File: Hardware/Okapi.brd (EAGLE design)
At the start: 64.8 x 100 mm, 215 parts, among them IC1 ATMEGA1284M, J1 CONN_82.54_SCREW, J3 CONN_42.54_SCREW, J4 CONN_82.54_SCREW, Q1 DMG3404, Q2 DMG3404, Q3 FDN360P, Q4 2N7002, Q5 FDN360P, Q6 DMG3404, Q7 2N7002, Q8 2N7002, U1 TLV61220DBV, U10 TPS22917DBV, U11 SN74AUP1G04YFP, U12 SN74AUP1G04YFP, U13 SN74AUP1G04YFP, U14 SN74AUP2G08DQE, U15 SN74AUP2G08DQE, U16 SN74AUP2G08DQE, U17 MIC2544MSOP, U18 MIC2544MSOP, U19 MIC2544MSOP, U2 TPS62822DLC, U20 MIC2544MSOP, U21 TPS22917DBV, U22 TPS22917DBV, U23 FT231X-Q, U24 SN74LVC1G3157DRL, U25 SN74AUP3G34DCU, U26 TXS0102DQM, U27 TXS0104RGY, U28 TCA9406DCU, U29 TXS0104RGY, U3 TPS61032RSA, U30 MCP4726A2SOT-23, U31 BME280, U32 ADS1115, U33 ADS1115, U34 INA211DCK, U35 INA213DCK, U36 TCA9406DCU, U37 TLV3691DCK, U38 TS5A21366RSE, U39 MIC94094C6, U40 SN74AHC1G86DCK, U41 MCP23018QFN, U42 TXS0104RGY, U5 BQ2980RUG, U6 TPS2105, U7 LTC4412S6, U8 TPL5111DDC, U9 TPS79733

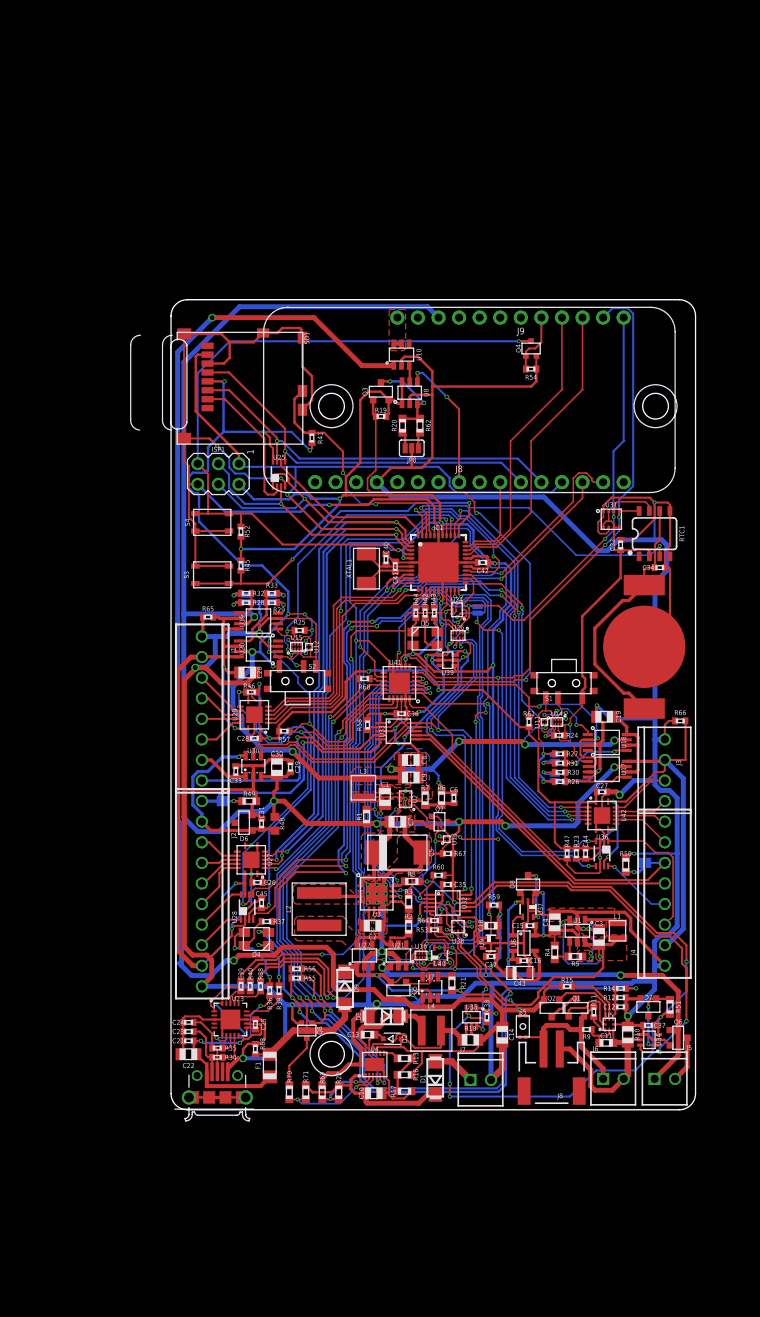
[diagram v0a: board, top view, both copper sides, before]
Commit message: Updated layout
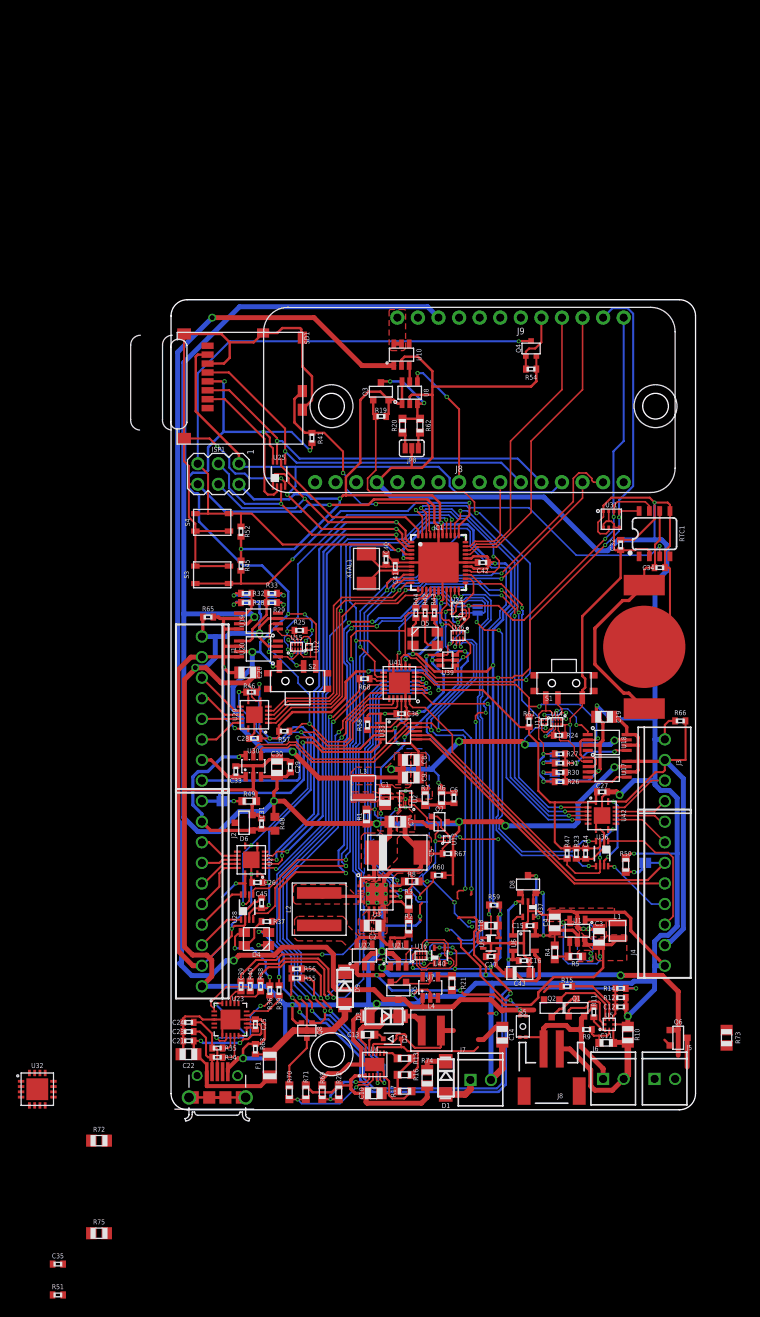
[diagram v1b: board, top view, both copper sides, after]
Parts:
- removed C37, C38: 0.1uF, bschulz_passives:C0402
- removed D7: (no value), bschulz:SOT23-3
- removed R18: 50m, bschulz_passives:R0805
- removed R53, R64: 1M, bschulz_passives:R0402
- removed U34: INA211DCK, bschulz:DCK_R-PDSO-G6
- removed U35: INA213DCK, bschulz:DCK_R-PDSO-G6
- removed U38: TS5A21366RSE, bschulz:RSE0008A
- added R72, R73, R74, R75: (no value), bschulz_passives:R0805
- R51: value 20k -> (none); device bschulz_passives:R0603 -> bschulz_passives:R0402
- U32: value ADS1115 -> PAC1934QFN; device bschulz:VSSOP_10 -> bschulz:QFN16
- moved R51 83.5 mm to (-14.0, -22.9), turned to 0 degrees
- moved C35 67.2 mm to (-14.0, -19.1), turned to 0 degrees
- moved U32 55.6 mm to (-16.5, 2.54), turned to 0 degrees
- moved D1 1.27 mm to (33.9, 3.94), turned to 270 degrees
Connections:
- removed net I_LI: U32.7, U34.6
- removed net I_SOLAR: U32.5, U35.6
- removed net SOLAR_SENSE+: L4.P$2, R18.1, U35.4, U4.10
- new net CSA_!ALERT: U32.1, U41.4
- new net V_BETA_SENSE: D9.C, Q5.2, R75.1, U32.10
- new net V_SOLAR_SENSE: D1.C, R74.1, U32.8
- net 3V3_CORE: now also C35.1, U32.15, U32.16, U32.2
- net 5V_AUX: no longer C35.1, C37.1, C38.1, R51.2, U32.8, U34.3, U35.3, U38.2
- net ADC_OB_ALERT: no longer U32.2, U41.4
- net ADC_SENSE_SW: no longer U38.3, U38.7
- net GND: now also R51.1, U32.EP; no longer C37.2, C38.2, D7.2, R53.1, R64.1, U32.1, U34.2, U34.4, U35.1, U35.2, U38.6
- net LI-: no longer U34.5
- net N$21: now also R51.2, U32.6; no longer D7.1, R51.1, U34.1
- net SCL: now also U32.4
- net SCL_5V: no longer U32.10
- net SDA_5V: no longer U32.9
- net SDA_OB: now also U32.5
- net V_BETA: now also R75.2, U32.9; no longer D9.C, Q5.2
- net V_LI: now also L4.P$2, R72.2, U32.11, U4.10; no longer Q2.2, R18.2, U35.5, U38.8
- net V_LI_SENSE: now also Q2.2, R72.1, U32.12; no longer R64.2, U32.4, U38.1
- net V_PRIME: now also R73.2, U32.14; no longer J5.P2, U38.4
- net V_PRIME_SENSE: now also J5.P2, R73.1, U32.13; no longer R53.2, U32.6, U38.5
- net V_SOLAR_IN: now also R74.2, U32.7; no longer D1.C
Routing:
- net 5V_AUX: track 343.4 -> 246.4 mm, vias 18 -> 13
- net I_LI: track 48.5 -> 0.00 mm, vias 2 -> 0
- net GND: track 910.3 -> 888.0 mm
- net I_SOLAR: track 19.8 -> 0.00 mm, vias 2 -> 0
- net SOLAR_SENSE+: track 18.3 -> 0.00 mm
- net V_PRIME_SENSE: track 12.5 -> 0.00 mm, vias 2 -> 0
- net N$21: track 9.40 -> 0.00 mm, vias 2 -> 0
- net V_LI_SENSE: track 8.45 -> 0.00 mm, vias 2 -> 0
- net V_BETA: track 64.1 -> 56.6 mm
- net V_LI: track 206.9 -> 213.0 mm
- net V_PRIME: track 76.1 -> 71.6 mm
- net V_BETA_SENSE: track 0.00 -> 4.16 mm
- net V_SOLAR_SENSE: track 0.00 -> 3.30 mm
- net V_PRIME-: track 5.69 -> 3.60 mm
- net ADC_OB_ALERT: track 42.5 -> 41.0 mm
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
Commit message: Continued layout updates
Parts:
- moved R72 55.0 mm to (43.4, 13.1), turned to 180 degrees
- moved R75 44.9 mm to (24.1, 15.2)
- moved R73 9.41 mm to (59.2, 9.27), turned to 90 degrees
- moved Q5 8.75 mm to (20.3, 18.8), turned to 0 degrees
- moved C14 4.33 mm to (36.6, 9.65)
- moved R38 1.27 mm to (9.78, 15.2)
- moved R40 1.14 mm to (10.9, 15.2)
- moved D9 0.92 mm to (21.0, 14.2)
- moved C13 0.25 mm to (24.3, 9.02)
- moved D3 0.25 mm to (26.3, 11.3)
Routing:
- net N$45: track 3.80 -> 18.2 mm
- net V_LI: track 213.0 -> 202.6 mm, vias 4 -> 2
- net GND: track 888.0 -> 897.1 mm
- net TX: track 103.6 -> 95.3 mm
- net 3V3_CORE: track 271.4 -> 279.1 mm
- net V_PRIME: track 71.6 -> 65.9 mm
- net RX: track 106.4 -> 101.2 mm
- net V_BETA: track 56.6 -> 61.4 mm, vias 4 -> 6
- net V_PRIME_SENSE: track 0.00 -> 4.72 mm
- net VUSB_POWER: track 63.9 -> 59.6 mm
- net V_BETA_SENSE: track 4.16 -> 1.47 mm, vias 0 -> 1
- net MPPT_FAULT: track 65.8 -> 63.4 mm
- net MPPT_CHRG: track 66.6 -> 64.5 mm
- net V_PRIME-: track 3.60 -> 5.69 mm
- net N$47: track 7.43 -> 8.65 mm
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
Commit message: CSA layout
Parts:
- removed R60: 100k, bschulz_passives:R0402
- moved C35 68.3 mm to (34.8, 28.8), turned to 180 degrees
- moved R51 66.2 mm to (31.1, 25.7), turned to 90 degrees
- moved U32 56.2 mm to (34.8, 25.4), turned to 270 degrees
- moved C18 0.36 mm to (39.8, 23.0)
- moved U9 0.25 mm to (39.8, 20.6)
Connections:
- removed net ADC_OB_ALERT: R60.1
- net 5V_AUX: no longer R60.2
- net V_BETA: now also U32.7; no longer U32.9
- net V_BETA_SENSE: now also U32.8; no longer U32.10
- net V_LI: now also U32.13; no longer U32.11
- net V_LI_SENSE: now also U32.14; no longer U32.12
- net V_PRIME: now also U32.12; no longer U32.14
- net V_PRIME_SENSE: now also U32.11; no longer U32.13
- net V_SOLAR_IN: now also U32.9; no longer U32.7
- net V_SOLAR_SENSE: now also U32.10; no longer U32.8
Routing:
- net ADC_SENSE_SW: track 66.4 -> 0.00 mm, vias 5 -> 0
- net SDA_OB: track 78.6 -> 122.1 mm, vias 4 -> 6
- net ADC_OB_ALERT: track 41.0 -> 0.00 mm, vias 2 -> 0
- net V_PRIME_SENSE: track 4.72 -> 37.4 mm, vias 0 -> 2
- net CSA_!ALERT: track 0.00 -> 32.3 mm, vias 0 -> 2
- net V_BETA_SENSE: track 1.47 -> 30.7 mm, vias 1 -> 2
- net V_BETA: track 61.4 -> 87.5 mm, vias 6 -> 7
- net V_SOLAR_IN: track 22.4 -> 48.0 mm, vias 0 -> 2
- net SDA_5V: track 65.9 -> 40.6 mm, vias 3 -> 2
- net V_SOLAR_SENSE: track 3.30 -> 28.4 mm, vias 0 -> 2
- net SCL_5V: track 67.9 -> 44.0 mm, vias 3 -> 2
- net V_PRIME: track 65.9 -> 87.7 mm, vias 5 -> 6
- net V_LI_SENSE: track 0.00 -> 18.8 mm
- net V_LI: track 202.6 -> 220.1 mm
- net SCL: track 173.3 -> 185.8 mm, vias 6 -> 7
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
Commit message: Design updates toward v1.0
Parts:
- removed USB1: MICRO_USB_LONGPADS, bschulz:10118194-0001LF_10118194-0001LF_LONGER_PADS
- added C37, C38, C46, C47, C48, C50, C57: 0.1uF, bschulz_passives:C0402
- added D10, D13, D16: LEDGREEN0603, bschulz:LED_0603
- added D11, D14, D17: LEDYELLOW0603, bschulz:LED_0603
- added D12, D18: LEDRED0603, bschulz:LED_0603
- added D7: CLVBA-FKA, bschulz:CLVBA-FKA
- added F2: (no value), bschulz:1206
- added J10: (no value), microbuilder:USB_C_CUSB31-CFM2AX-01-X
- added J9: B_SERIES_M.2EKEY_NOPROG, bschulz:PARTICLE_M.2EKEY_NOPROG
- added R18: 100k, bschulz_passives:R0402
- added R53, R60, R64, R76, R77, R78, R79, R80: 220R, bschulz_passives:R0402
- added R81, R82, R83: 5.6k, bschulz_passives:R0402
- added R84, R85: (no value), bschulz_passives:R0402
- added U34: TXS0102DQM, bschulz:DQM_R-PX2SON-N8
- added U35: MB85RC, bschulz:SO08
- added U38: MLX90393, bschulz:QFN16_3X3
- added U43: BMA456, bschulz:LGA-12_2X2
- added U44: VEML6030, bschulz:VEML6030
- added U45: PCA9634QFN, bschulz:QFN20_5X5
- added USB2: USB_MICROVERT, bschulz:USB_MICRO_VERT_MOLEX
- D8, Q3, Q5: device bschulz:SOT23-3 -> bschulz:SOT23-3@1
- F1: value PPTC1.5A -> (none)
- moved Q4 20.3 mm to (24.1, 94.0), turned to 90 degrees
- moved R54 18.0 mm to (26.7, 94.0), turned to 270 degrees
- moved C21 12.0 mm to (14.0, 6.22), turned to 270 degrees
- moved C22 10.2 mm to (12.3, 6.73), turned to 270 degrees
- moved JP8 6.93 mm to (30.7, 88.5), turned to 270 degrees
- moved R62 5.80 mm to (27.9, 89.5), turned to 180 degrees
- moved U10 5.57 mm to (24.6, 97.3), turned to 270 degrees
- moved Q3 5.12 mm to (23.4, 84.2)
- moved U8 5.08 mm to (24.4, 88.5)
- moved R19 4.58 mm to (23.4, 81.8)
- moved R63 4.49 mm to (13.7, 10.5)
- moved F1 3.74 mm to (15.7, 6.60)
- moved R20 2.99 mm to (27.9, 87.4), turned to 180 degrees
- moved R35 2.25 mm to (5.08, 9.78)
- moved R34 2.25 mm to (5.08, 8.64)
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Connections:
- removed net ADC_SENSE_SW: IC1.40
- removed net N$1: USB1.BODY@1, USB1.BODY@2, USB1.BODY@3, USB1.BODY@4, USB1.BODY@7, USB1.BODY@8
- removed net N$48: C24.2, R35.2, USB1.3
- removed net N$49: C23.2, R34.2, USB1.2
- new net !LED_EN: IC1.40, R18.1, U45.13
- new net 3V3_FEATHER: C37.1, D7.2, MS1.2, U34.5, U34.8
- new net BLUE: J9.65, R83.2
- new net BSOM_VUSB: F2.1, J9.16, USB2.1
- new net CC1: J10.A5, R85.2
- new net CC2: J10.B5, R84.2
- new net D+: C24.2, J10.A6, J10.B6, R35.2
- new net D-: C23.2, J10.A7, J10.B7, R34.2
- new net GREEN: J9.63, R82.2
- new net N$25: D10.CATHODE, U45.4
- new net N$67: D11.CATHODE, U45.5
- new net N$70: D12.CATHODE, U45.6
- new net N$71: D13.CATHODE, U45.7
- new net N$72: D14.CATHODE, U45.9
- new net N$73: D16.CATHODE, U45.10
- new net N$74: D17.CATHODE, U45.11
- new net N$75: D18.CATHODE, U45.12
- new net N$76: D10.ANODE, R53.1
- new net N$77: D11.ANODE, R60.1
- new net N$78: D12.ANODE, R64.1
- new net N$79: D13.ANODE, R76.1
- new net N$80: D14.ANODE, R77.1
- new net N$81: D16.ANODE, R78.1
- new net N$82: D17.ANODE, R79.1
- new net N$83: D18.ANODE, R80.1
- new net N$84: D7.1, R81.1
- new net N$85: D7.4, R82.1
- new net N$86: D7.3, R83.1
- new net PD+: J9.11, USB2.3
- new net PD-: J9.13, USB2.2
- new net RED: J9.61, R81.2
- new net SBU1: J10.A8
- new net SBU2: J10.B8
- new net SCL_FEATHER: J9.20, MS1.18, U34.6
- new net SDA_FEATHER: J9.22, MS1.17, U34.7
- new net SENSOR_INT: U43.5
- new net SIM_VCC: J9.67
- new net UB_VBUS: J9.74
- net 3V3_AUX: now also C38.1, C46.1, C47.1, C48.1, C57.1, J9.10, J9.12, U38.15, U38.2, U38.8, U43.10, U43.3, U43.7, U44.4, U44.6
- net 3V3_CORE: now also C50.1, R18.2, R53.2, R60.2, R64.2, R76.2, R77.2, R78.2, R79.2, R80.2, U34.1, U35.8, U45.15, U45.18, U45.20, U45.3
- net 5V_AUX: now also F2.2
- net FEATHER_BAT: now also J9.2, J9.4, J9.6, J9.8
- net FEATHER_CTS: now also J9.40
- net FEATHER_GPIO: now also J9.43
- net FEATHER_RTS: now also J9.42
- net GND: now also C37.2, C38.2, C46.2, C47.2, C48.2, C50.2, C57.2, J10.A1B12, J10.B1A12, J9.1, J9.15, J9.21, J9.3, J9.39, J9.49, J9.5, J9.56, J9.7, J9.76, J9.77, J9.9, J9.GND, R84.1, R85.1, U34.4, U35.1, U35.2, U35.3, U35.4, U35.7, U38.10, U38.11, U38.12, U38.13, U38.14, U38.16, U38.4, U38.9, U38.EP, U43.1, U43.8, U43.9, U44.1, U45.1, U45.14, U45.19, U45.2, U45.8, U45.EP, USB2.5; no longer USB1.5
- net MISO: now also J9.50
- net MOSI_BUF: now also J9.52
- net RST_TRIG: now also J9.66
- net RX: now also J9.36
- net SCK_BUF: now also J9.54
- net SCL: now also U34.3, U35.6, U38.3, U43.12, U44.5, U45.16; no longer MS1.18
- net SDA_OB: now also U34.2, U35.5, U38.5, U43.2, U44.2, U45.17; no longer MS1.17
- net TX: now also J9.38
- net VUSB: now also J10.A4B9, J10.B4A9; no longer USB1.1
- net WD_DONE: now also J9.37
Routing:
- net GND: track 908.3 -> 1007.9 mm, vias 41 -> 46
- net 3V3_AUX: track 224.8 -> 290.7 mm, vias 20 -> 24
- net 3V3_CORE: track 287.0 -> 340.3 mm, vias 23 -> 24
- net !LED_EN: track 0.00 -> 50.8 mm, vias 0 -> 3
- net SDA_FEATHER: track 0.00 -> 30.9 mm
- net SCL_FEATHER: track 0.00 -> 25.8 mm
- net RST: track 169.1 -> 147.2 mm
- net 3V3_FEATHER: track 0.00 -> 17.8 mm, vias 0 -> 4
- net RX: track 101.2 -> 118.1 mm
- net RST_TRIG: track 7.59 -> 23.3 mm
- net TX: track 95.3 -> 110.1 mm
- net FEATHER_RTS: track 36.9 -> 51.0 mm, vias 0 -> 1
- net SDA_OB: track 122.1 -> 134.0 mm, vias 6 -> 8
- net N$75: track 0.00 -> 10.9 mm
- net FAULT_SEC: track 37.0 -> 47.2 mm, vias 2 -> 3
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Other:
- board size 64.8 x 100 mm -> 64.8 x 135 mm
- board text added: "1"
- board text added: "2"
- board text added: "3"
- board text added: "A"
- board text added: "B"
- board text added: "C"
- board text added: "Project Okapi v1.0 ---------------- Developed by Northern Widget and University of Minnesota"
- board text removed: "Project Okapi v0.6 ---------------- Developed by Northern Widget and University of Minnesota"

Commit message: Continued design updates
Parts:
- moved USB2 142.1 mm to (62.2, 104.1), turned to 90 degrees
- moved F2 124.3 mm to (27.4, 102.7), turned to 270 degrees
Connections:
- net 3V3_AUX: no longer J9.10, J9.12
- net 3V3_FEATHER: now also J9.10, J9.12
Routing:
- net GND: track 1007.9 -> 1092.6 mm, vias 46 -> 47
- net BSOM_VUSB: track 0.00 -> 55.4 mm, vias 0 -> 3
- net 3V3_FEATHER: track 17.8 -> 69.8 mm, vias 4 -> 5
- net FEATHER_BAT: track 0.95 -> 34.5 mm, vias 0 -> 1
- net 3V3_CORE: track 340.3 -> 372.1 mm, vias 24 -> 26
- net PD+: track 0.00 -> 27.6 mm
- net PD-: track 0.00 -> 26.3 mm
- net WD_DONE: track 21.6 -> 39.3 mm, vias 2 -> 3
- net MISO: track 134.4 -> 151.9 mm, vias 3 -> 4
- net MOSI_BUF: track 48.6 -> 65.0 mm, vias 1 -> 3
- net SCK_BUF: track 47.2 -> 60.8 mm, vias 1 -> 3
- net 5V_AUX: track 239.6 -> 246.6 mm
- net FEATHER_GPIO: track 11.4 -> 17.8 mm
- net FEATHER_RTS: track 51.0 -> 47.3 mm, vias 1 -> 2
- net RST_TRIG: track 23.3 -> 26.4 mm
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
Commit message: v1.0 updates
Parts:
- added R86, R87: (no value), bschulz_passives:R0402
- added S6, S7: BUTTON4.2X3.2, bschulz:SWITCH_4.2X3.2
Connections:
- new net !MODE: J9.32, R87.1, S6.1, S6.2
- new net !RST: J9.34, R86.1, S7.1, S7.2
- net 3V3_FEATHER: now also R86.2, R87.2
- net GND: now also S6.3, S6.4, S7.3, S7.4
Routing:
- net GND: track 1092.6 -> 1161.7 mm
- net !MODE: track 0.00 -> 49.0 mm, vias 0 -> 2
- net !RST: track 0.00 -> 46.2 mm, vias 0 -> 2
- net 3V3_FEATHER: track 69.8 -> 112.1 mm, vias 5 -> 6
- net BSOM_VUSB: track 55.4 -> 61.5 mm
- net 5V_AUX: track 246.6 -> 247.7 mm
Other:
- board text added: "MODE"
- board text added: "No Cover!"
